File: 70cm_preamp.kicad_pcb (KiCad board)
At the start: 2 copper layers, 33.4 x 13.2 mm, 4 parts, among them J1 RF_IN, J2 RF_OUT, U1 SF2446E, U2 PGA-103+

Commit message: Feliratok
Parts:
- added G***: LOGO, 70cm_preamp:RCV, B.Cu at (47.6, 31.7)
- added G***: LOGO, 70cm_preamp:ANT, B.Cu at (70.6, 31.7)
- added G***: LOGO, 70cm_preamp:HA5KFU, F.Cu at (59.1, 31.4)
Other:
- board text removed: "ANT"
- board text removed: "HA5KFU"
- board text removed: "RCV"

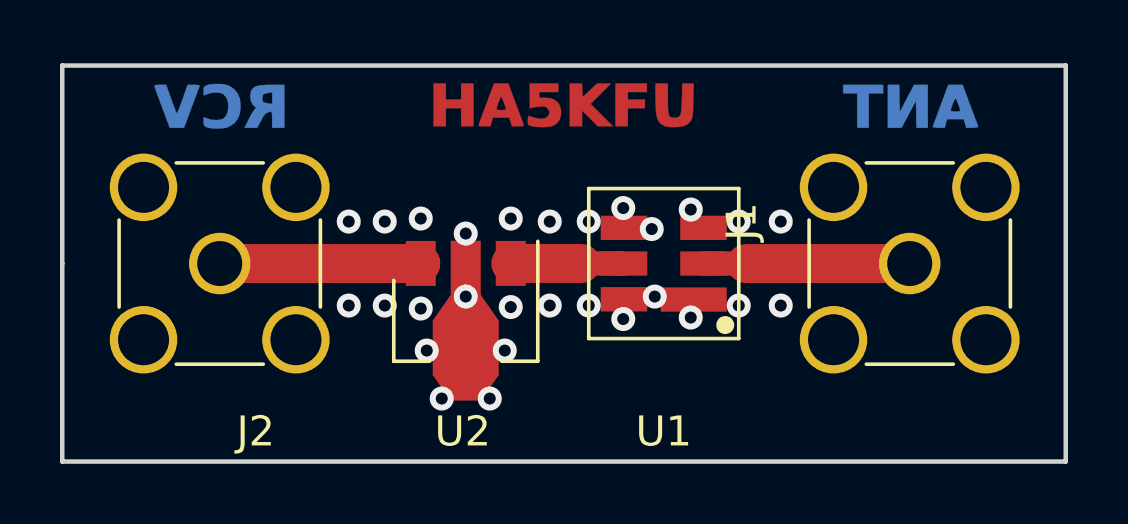
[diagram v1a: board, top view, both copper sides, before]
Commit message: Change via size
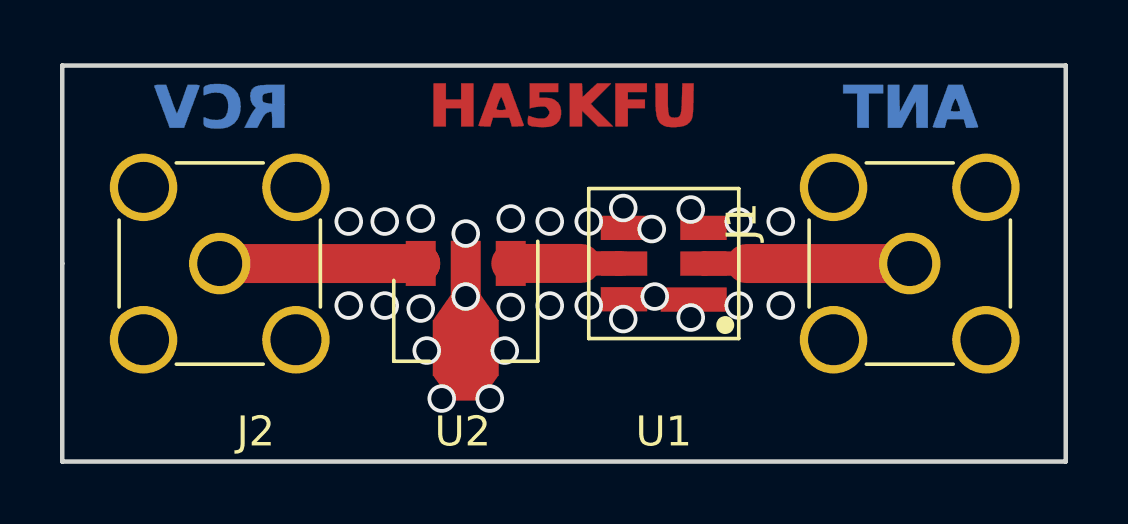
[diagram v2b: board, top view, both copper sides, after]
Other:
- net class Default: via_dia 0.8 -> 0.95; via_drill 0.4 -> 0.7
- net class Tapvonal_vastag: via_dia 0.8 -> 0.95; via_drill 0.4 -> 0.7
- net class Tapvonal_vekony: via_dia 0.8 -> 0.95; via_drill 0.4 -> 0.7
- rule via_min_drill: 0.3 -> 0.7
- rule via_min_size: 0.4 -> 0.8
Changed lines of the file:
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@@
     (zone_45_only no)
     (trace_min 0.2)
-    (via_size 0.8)
-    (via_drill 0.4)
-    (via_min_size 0.4)
-    (via_min_drill 0.3)
+    (via_size 0.95)
+    (via_drill 0.7)
+    (via_min_size 0.8)
+    (via_min_drill 0.7)
     (uvia_size 0.3)
     (uvia_drill 0.1)
@@
     (clearance 0.2)
     (trace_width 0.25)
-    (via_dia 0.8)
-    (via_drill 0.4)
+    (via_dia 0.95)
+    (via_drill 0.7)
     (uvia_dia 0.3)
     (uvia_drill 0.1)
@@
     (clearance 0.33)
     (trace_width 1.3)
-    (via_dia 0.8)
-    (via_drill 0.4)
+    (via_dia 0.95)
+    (via_drill 0.7)
     (uvia_dia 0.3)
     (uvia_drill 0.1)
@@
     (clearance 0.12)
     (trace_width 0.81)
-    (via_dia 0.8)
-    (via_drill 0.4)
+    (via_dia 0.95)
+    (via_drill 0.7)
     (uvia_dia 0.3)
     (uvia_drill 0.1)
@@
   (segment (start 54.2965 36.8) (end 54.3 36.7965) (width 1.3) (layer F.Cu) (net 1))
   (segment (start 47.6 36.8) (end 54.2965 36.8) (width 1.3) (layer F.Cu) (net 1))
-  (via (at 54.3 35.3) (size 0.8) (drill 0.4) (layers F.Cu B.Cu) (net 2))
-  (via (at 53.1 35.4) (size 0.8) (drill 0.4) (layers F.Cu B.Cu) (net 2))
-  (via (at 53.1 38.2) (size 0.8) (drill 0.4) (layers F.Cu B.Cu) (net 2))
-  (via (at 54.3 38.3) (size 0.8) (drill 0.4) (layers F.Cu B.Cu) (net 2))
-  (via (at 57.3 35.3) (size 0.8) (drill 0.4) (layers F.Cu B.Cu) (net 2))
-  (via (at 57.3 38.25) (size 0.8) (drill 0.4) (layers F.Cu B.Cu) (net 2))
-  (via (at 62.1 37.9) (size 0.8) (drill 0.4) (layers F.Cu B.Cu) (net 2))
-  (via (at 62 35.65) (size 0.8) (drill 0.4) (layers F.Cu B.Cu) (net 2))
-  (via (at 63.3 35) (size 0.8) (drill 0.4) (layers F.Cu B.Cu) (net 2))
-  (via (at 63.3 38.6) (size 0.8) (drill 0.4) (layers F.Cu B.Cu) (net 2))
-  (via (at 59.9 38.2) (size 0.8) (drill 0.4) (layers F.Cu B.Cu) (net 2))
-  (via (at 59.9 35.4) (size 0.8) (drill 0.4) (layers F.Cu B.Cu) (net 2))
-  (via (at 58.6 38.2) (size 0.8) (drill 0.4) (layers F.Cu B.Cu) (net 2))
-  (via (at 51.9 38.2) (size 0.8) (drill 0.4) (layers F.Cu B.Cu) (net 2))
-  (via (at 51.9 35.4) (size 0.8) (drill 0.4) (layers F.Cu B.Cu) (net 2))
-  (via (at 55.8 37.9) (size 0.8) (drill 0.4) (layers F.Cu B.Cu) (net 2))
-  (via (at 54.5 39.7) (size 0.8) (drill 0.4) (layers F.Cu B.Cu) (net 2))
-  (via (at 57.1 39.7) (size 0.8) (drill 0.4) (layers F.Cu B.Cu) (net 2))
-  (via (at 55 41.3) (size 0.8) (drill 0.4) (layers F.Cu B.Cu) (net 2))
-  (via (at 56.6 41.3) (size 0.8) (drill 0.4) (layers F.Cu B.Cu) (net 2))
-  (via (at 61.05 38.65) (size 0.8) (drill 0.4) (layers F.Cu B.Cu) (net 2))
-  (via (at 61.05 34.95) (size 0.8) (drill 0.4) (layers F.Cu B.Cu) (net 2))
-  (via (at 55.8 35.8) (size 0.8) (drill 0.4) (layers F.Cu B.Cu) (net 2))
-  (via (at 58.6 35.4) (size 0.8) (drill 0.4) (layers F.Cu B.Cu) (net 2))
-  (via (at 64.9 38.2) (size 0.8) (drill 0.4) (layers F.Cu B.Cu) (net 2))
-  (via (at 64.9 35.4) (size 0.8) (drill 0.4) (layers F.Cu B.Cu) (net 2))
-  (via (at 66.3 35.4) (size 0.8) (drill 0.4) (layers F.Cu B.Cu) (net 2))
-  (via (at 66.3 38.2) (size 0.8) (drill 0.4) (layers F.Cu B.Cu) (net 2))
+  (via (at 54.3 35.3) (size 0.95) (drill 0.7) (layers F.Cu B.Cu) (net 2))
+  (via (at 53.1 35.4) (size 0.95) (drill 0.7) (layers F.Cu B.Cu) (net 2))
+  (via (at 53.1 38.2) (size 0.95) (drill 0.7) (layers F.Cu B.Cu) (net 2))
+  (via (at 54.3 38.3) (size 0.95) (drill 0.7) (layers F.Cu B.Cu) (net 2))
+  (via (at 57.3 35.3) (size 0.95) (drill 0.7) (layers F.Cu B.Cu) (net 2))
+  (via (at 57.3 38.25) (size 0.95) (drill 0.7) (layers F.Cu B.Cu) (net 2))
+  (via (at 62.1 37.9) (size 0.95) (drill 0.7) (layers F.Cu B.Cu) (net 2))
+  (via (at 62 35.65) (size 0.95) (drill 0.7) (layers F.Cu B.Cu) (net 2))
+  (via (at 63.3 35) (size 0.95) (drill 0.7) (layers F.Cu B.Cu) (net 2))
+  (via (at 63.3 38.6) (size 0.95) (drill 0.7) (layers F.Cu B.Cu) (net 2))
+  (via (at 59.9 38.2) (size 0.95) (drill 0.7) (layers F.Cu B.Cu) (net 2))
+  (via (at 59.9 35.4) (size 0.95) (drill 0.7) (layers F.Cu B.Cu) (net 2))
+  (via (at 58.6 38.2) (size 0.95) (drill 0.7) (layers F.Cu B.Cu) (net 2))
+  (via (at 51.9 38.2) (size 0.95) (drill 0.7) (layers F.Cu B.Cu) (net 2))
+  (via (at 51.9 35.4) (size 0.95) (drill 0.7) (layers F.Cu B.Cu) (net 2))
+  (via (at 55.8 37.9) (size 0.95) (drill 0.7) (layers F.Cu B.Cu) (net 2))
+  (via (at 54.5 39.7) (size 0.95) (drill 0.7) (layers F.Cu B.Cu) (net 2))
+  (via (at 57.1 39.7) (size 0.95) (drill 0.7) (layers F.Cu B.Cu) (net 2))
+  (via (at 55 41.3) (size 0.95) (drill 0.7) (layers F.Cu B.Cu) (net 2))
+  (via (at 56.6 41.3) (size 0.95) (drill 0.7) (layers F.Cu B.Cu) (net 2))
+  (via (at 61.05 38.65) (size 0.95) (drill 0.7) (layers F.Cu B.Cu) (net 2))
+  (via (at 61.05 34.95) (size 0.95) (drill 0.7) (layers F.Cu B.Cu) (net 2))
+  (via (at 55.8 35.8) (size 0.95) (drill 0.7) (layers F.Cu B.Cu) (net 2))
+  (via (at 58.6 35.4) (size 0.95) (drill 0.7) (layers F.Cu B.Cu) (net 2))
+  (via (at 64.9 38.2) (size 0.95) (drill 0.7) (layers F.Cu B.Cu) (net 2))
+  (via (at 64.9 35.4) (size 0.95) (drill 0.7) (layers F.Cu B.Cu) (net 2))
+  (via (at 66.3 35.4) (size 0.95) (drill 0.7) (layers F.Cu B.Cu) (net 2))
+  (via (at 66.3 38.2) (size 0.95) (drill 0.7) (layers F.Cu B.Cu) (net 2))
   (segment (start 70.6 36.8) (end 65.15 36.8) (width 1.3) (layer F.Cu) (net 3))
   (segment (start 63.75 36.8) (end 65.15 36.8) (width 0.81) (layer F.Cu) (net 3))

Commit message: viák
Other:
- board size 33.4 x 13.2 mm -> 33 x 13.2 mm
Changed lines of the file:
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@@
-(kicad_pcb (version 20171130) (host pcbnew 5.1.6-c6e7f7d~86~ubuntu19.10.1)
+(kicad_pcb (version 20171130) (host pcbnew 5.1.5+dfsg1-2build2)
   (general
     (thickness 1.6)
@@
     )
   )
-  (gr_line (start 42.35 43.4) (end 42.35 36.8) (layer Edge.Cuts) (width 0.15))
-  (gr_line (start 75.8 43.4) (end 42.35 43.4) (layer Edge.Cuts) (width 0.15))
-  (gr_line (start 75.8 30.2) (end 75.8 43.4) (layer Edge.Cuts) (width 0.15))
-  (gr_line (start 42.35 30.2) (end 75.8 30.2) (layer Edge.Cuts) (width 0.15))
-  (gr_line (start 42.35 36.8) (end 42.35 30.2) (layer Edge.Cuts) (width 0.15))
+  (gr_line (start 42.6 43.4) (end 42.6 36.8) (layer Edge.Cuts) (width 0.15))
+  (gr_line (start 75.6 43.4) (end 42.6 43.4) (layer Edge.Cuts) (width 0.15))
+  (gr_line (start 75.6 30.2) (end 75.6 43.4) (layer Edge.Cuts) (width 0.15))
+  (gr_line (start 42.6 30.2) (end 75.6 30.2) (layer Edge.Cuts) (width 0.15))
+  (gr_line (start 42.6 36.8) (end 42.6 30.2) (layer Edge.Cuts) (width 0.15))
   (segment (start 54.2965 36.8) (end 54.3 36.7965) (width 1.3) (layer F.Cu) (net 1))
   (segment (start 47.6 36.8) (end 54.2965 36.8) (width 1.3) (layer F.Cu) (net 1))
-  (via (at 54.3 35.3) (size 0.95) (drill 0.7) (layers F.Cu B.Cu) (net 2))
-  (via (at 53.1 35.4) (size 0.95) (drill 0.7) (layers F.Cu B.Cu) (net 2))
-  (via (at 53.1 38.2) (size 0.95) (drill 0.7) (layers F.Cu B.Cu) (net 2))
-  (via (at 54.3 38.3) (size 0.95) (drill 0.7) (layers F.Cu B.Cu) (net 2))
-  (via (at 57.3 35.3) (size 0.95) (drill 0.7) (layers F.Cu B.Cu) (net 2))
-  (via (at 57.3 38.25) (size 0.95) (drill 0.7) (layers F.Cu B.Cu) (net 2))
-  (via (at 62.1 37.9) (size 0.95) (drill 0.7) (layers F.Cu B.Cu) (net 2))
-  (via (at 62 35.65) (size 0.95) (drill 0.7) (layers F.Cu B.Cu) (net 2))
-  (via (at 63.3 35) (size 0.95) (drill 0.7) (layers F.Cu B.Cu) (net 2))
-  (via (at 63.3 38.6) (size 0.95) (drill 0.7) (layers F.Cu B.Cu) (net 2))
-  (via (at 59.9 38.2) (size 0.95) (drill 0.7) (layers F.Cu B.Cu) (net 2))
-  (via (at 59.9 35.4) (size 0.95) (drill 0.7) (layers F.Cu B.Cu) (net 2))
-  (via (at 58.6 38.2) (size 0.95) (drill 0.7) (layers F.Cu B.Cu) (net 2))
-  (via (at 51.9 38.2) (size 0.95) (drill 0.7) (layers F.Cu B.Cu) (net 2))
-  (via (at 51.9 35.4) (size 0.95) (drill 0.7) (layers F.Cu B.Cu) (net 2))
+  (via (at 54.29 35.23) (size 0.95) (drill 0.7) (layers F.Cu B.Cu) (net 2))
+  (via (at 53.1 35.33) (size 0.95) (drill 0.7) (layers F.Cu B.Cu) (net 2))
+  (via (at 53.09 38.26) (size 0.95) (drill 0.7) (layers F.Cu B.Cu) (net 2))
+  (via (at 54.29 38.37) (size 0.95) (drill 0.7) (layers F.Cu B.Cu) (net 2))
+  (via (at 57.29 35.23) (size 0.95) (drill 0.7) (layers F.Cu B.Cu) (net 2))
+  (via (at 57.29 38.37) (size 0.95) (drill 0.7) (layers F.Cu B.Cu) (net 2))
+  (via (at 62.4 35.65) (size 0.95) (drill 0.7) (layers F.Cu B.Cu) (net 2))
+  (via (at 63.75 34.75) (size 0.95) (drill 0.7) (layers F.Cu B.Cu) (net 2))
+  (via (at 63.75 38.85) (size 0.95) (drill 0.7) (layers F.Cu B.Cu) (net 2))
+  (via (at 59.9 38.25) (size 0.95) (drill 0.7) (layers F.Cu B.Cu) (net 2))
+  (via (at 59.9 35.35) (size 0.95) (drill 0.7) (layers F.Cu B.Cu) (net 2))
+  (via (at 58.59 38.27) (size 0.95) (drill 0.7) (layers F.Cu B.Cu) (net 2))
+  (via (at 51.89 38.26) (size 0.95) (drill 0.7) (layers F.Cu B.Cu) (net 2))
+  (via (at 51.9 35.33) (size 0.95) (drill 0.7) (layers F.Cu B.Cu) (net 2))
   (via (at 55.8 37.9) (size 0.95) (drill 0.7) (layers F.Cu B.Cu) (net 2))
-  (via (at 54.5 39.7) (size 0.95) (drill 0.7) (layers F.Cu B.Cu) (net 2))
-  (via (at 57.1 39.7) (size 0.95) (drill 0.7) (layers F.Cu B.Cu) (net 2))
-  (via (at 55 41.3) (size 0.95) (drill 0.7) (layers F.Cu B.Cu) (net 2))
-  (via (at 56.6 41.3) (size 0.95) (drill 0.7) (layers F.Cu B.Cu) (net 2))
-  (via (at 61.05 38.65) (size 0.95) (drill 0.7) (layers F.Cu B.Cu) (net 2))
-  (via (at 61.05 34.95) (size 0.95) (drill 0.7) (layers F.Cu B.Cu) (net 2))
-  (via (at 55.8 35.8) (size 0.95) (drill 0.7) (layers F.Cu B.Cu) (net 2))
-  (via (at 58.6 35.4) (size 0.95) (drill 0.7) (layers F.Cu B.Cu) (net 2))
-  (via (at 64.9 38.2) (size 0.95) (drill 0.7) (layers F.Cu B.Cu) (net 2))
-  (via (at 64.9 35.4) (size 0.95) (drill 0.7) (layers F.Cu B.Cu) (net 2))
-  (via (at 66.3 35.4) (size 0.95) (drill 0.7) (layers F.Cu B.Cu) (net 2))
-  (via (at 66.3 38.2) (size 0.95) (drill 0.7) (layers F.Cu B.Cu) (net 2))
+  (via (at 54.3 39.7) (size 0.95) (drill 0.7) (layers F.Cu B.Cu) (net 2))
+  (via (at 57.3 39.7) (size 0.95) (drill 0.7) (layers F.Cu B.Cu) (net 2))
+  (via (at 54.7 41.3) (size 0.95) (drill 0.7) (layers F.Cu B.Cu) (net 2))
+  (via (at 56.9 41.3) (size 0.95) (drill 0.7) (layers F.Cu B.Cu) (net 2))
+  (via (at 61.05 38.85) (size 0.95) (drill 0.7) (layers F.Cu B.Cu) (net 2))
+  (via (at 61.05 34.75) (size 0.95) (drill 0.7) (layers F.Cu B.Cu) (net 2))
+  (via (at 55.8 35.6) (size 0.95) (drill 0.7) (layers F.Cu B.Cu) (net 2))
+  (via (at 58.59 35.33) (size 0.95) (drill 0.7) (layers F.Cu B.Cu) (net 2))
+  (via (at 65.04 38.27) (size 0.95) (drill 0.7) (layers F.Cu B.Cu) (net 2))
+  (via (at 65.04 35.33) (size 0.95) (drill 0.7) (layers F.Cu B.Cu) (net 2))
+  (via (at 66.44 35.33) (size 0.95) (drill 0.7) (layers F.Cu B.Cu) (net 2))
+  (via (at 66.44 38.27) (size 0.95) (drill 0.7) (layers F.Cu B.Cu) (net 2))
+  (via (at 62.4 38.85) (size 0.95) (drill 0.7) (layers F.Cu B.Cu) (net 2))
   (segment (start 70.6 36.8) (end 65.15 36.8) (width 1.3) (layer F.Cu) (net 3))
   (segment (start 63.75 36.8) (end 65.15 36.8) (width 0.81) (layer F.Cu) (net 3))
@@
     (polygon
       (pts
-        (xy 75.8 43.4) (xy 42.35 43.4) (xy 42.35 30.2) (xy 75.8 30.2)
+        (xy 75.6 43.4) (xy 42.6 43.4) (xy 42.6 30.2) (xy 75.6 30.2)
       )
     )
@@
     (polygon
       (pts
-        (xy 75.8 43.4) (xy 42.35 43.4) (xy 42.35 30.2) (xy 75.8 30.2)
+        (xy 75.6 43.4) (xy 42.6 43.4) (xy 42.6 30.2) (xy 75.6 30.2)
       )
     )
